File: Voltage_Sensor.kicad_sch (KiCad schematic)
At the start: 30 parts, among them U1 TLV9002QDRQ1

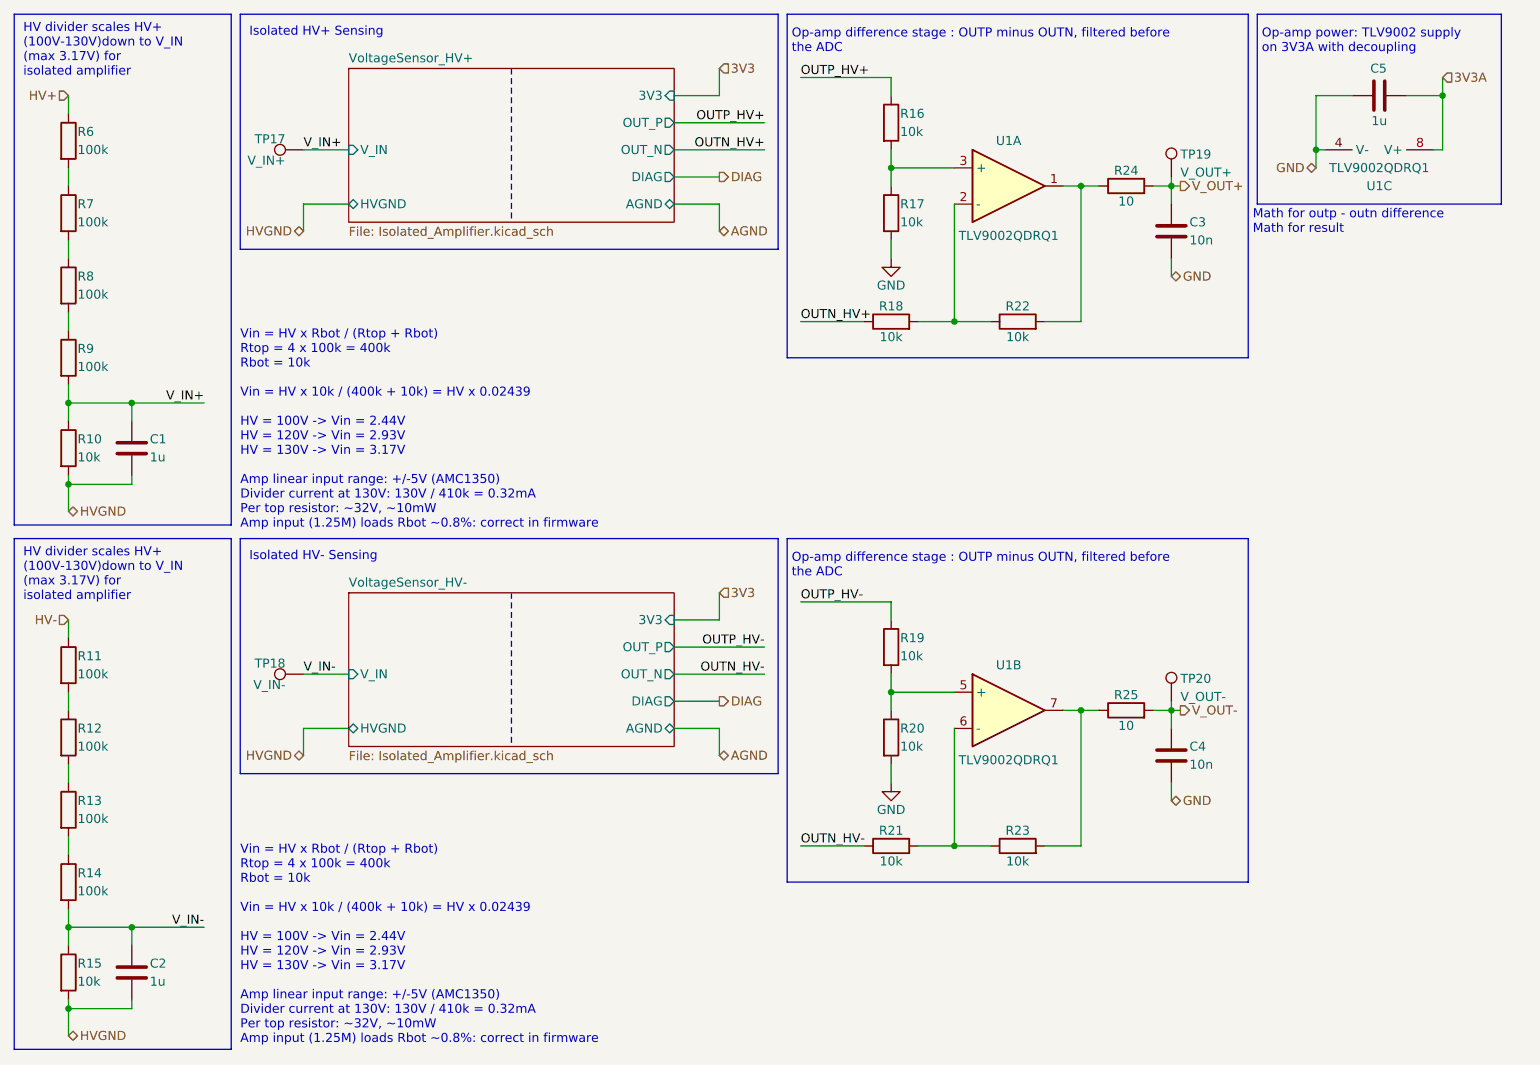
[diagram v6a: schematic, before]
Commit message: updated voltage divider to amc3311
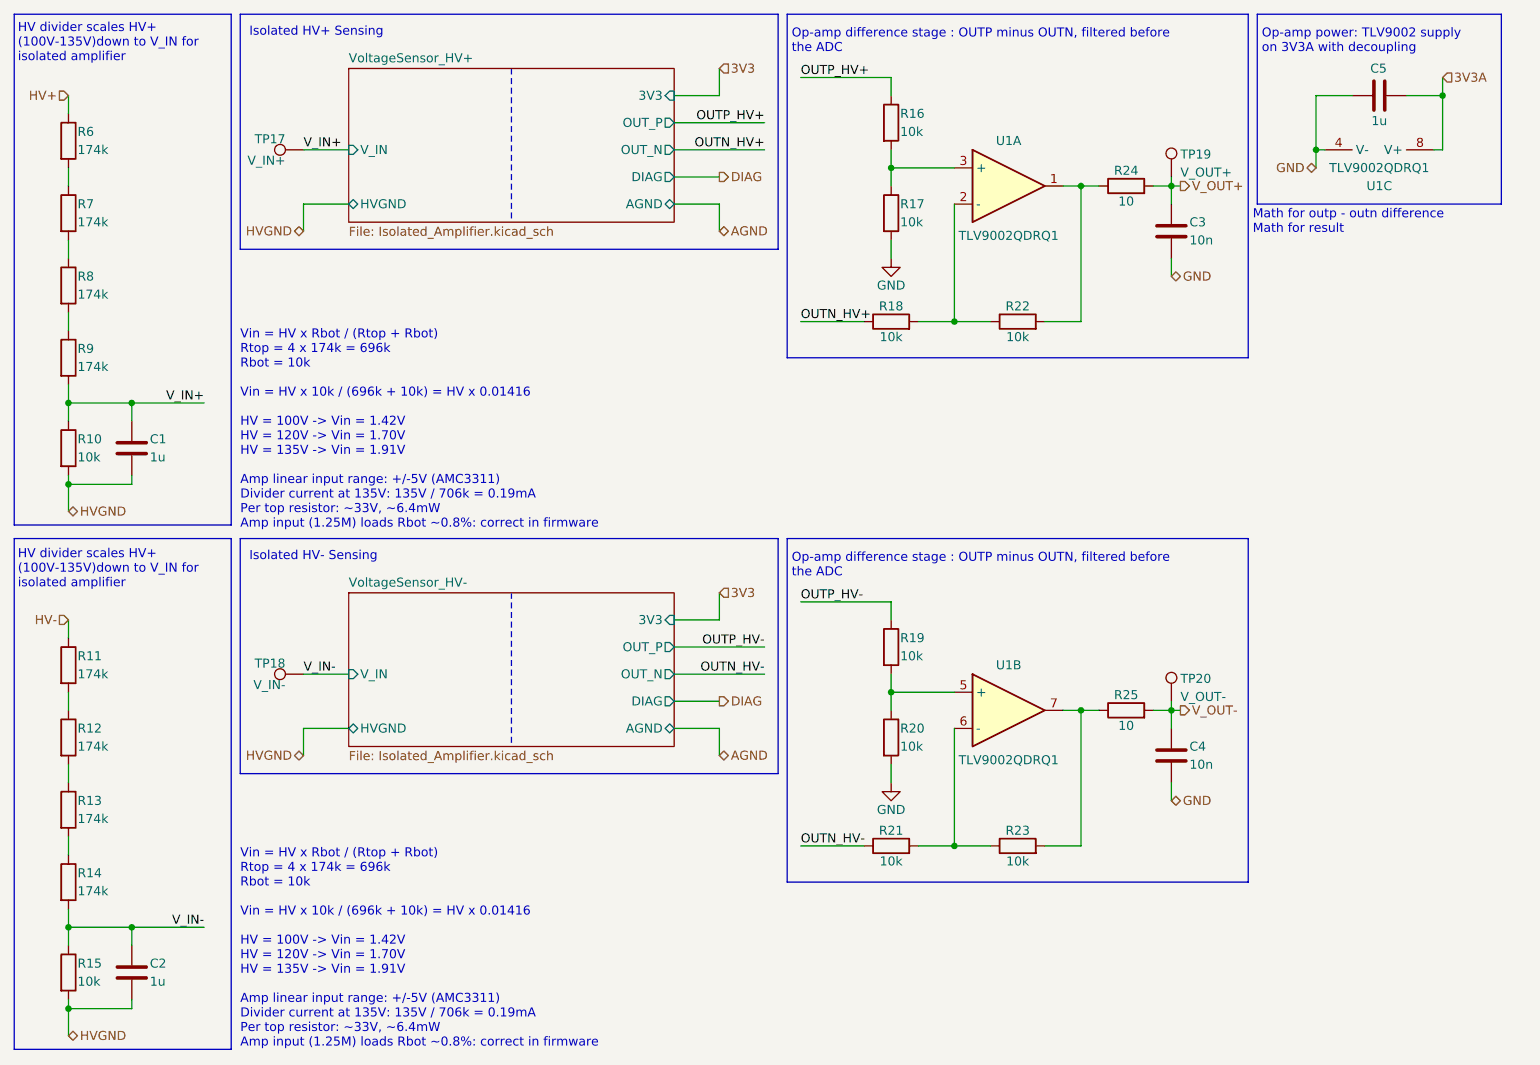
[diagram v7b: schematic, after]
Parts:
- R11, R12, R13, R14, R6, R7, R8, R9: value 100k -> 174k
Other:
- note added: "HV divider scales HV+ (100V-135V)down to V_IN for isolated amplifier"
- note added: "Vin = HV x Rbot / (Rtop + Rbot) Rtop = 4 x 174k = 696k Rbot = 10k Vin = HV x 10k / (696k + 10k) = HV x 0.01416 HV = 100V -> Vin = 1.42V HV = 120V -> Vin = 1.70V HV = 135V -> Vin = 1.91V Amp linear input range: +/-5V (AMC3311) Divider current at 135V: 135V / 706k = 0.19mA Per top resistor: ~33V, ~6.4mW Amp input (1.25M) loads Rbot ~0.8%: correct in firmware"
- note removed: "HV divider scales HV+ (100V-130V)down to V_IN (max 3.17V) for isolated amplifier"
- note removed: "Vin = HV x Rbot / (Rtop + Rbot) Rtop = 4 x 100k = 400k Rbot = 10k Vin = HV x 10k / (400k + 10k) = HV x 0.02439 HV = 100V -> Vin = 2.44V HV = 120V -> Vin = 2.93V HV = 130V -> Vin = 3.17V Amp linear input range: +/-5V (AMC1350) Divider current at 130V: 130V / 410k = 0.32mA Per top resistor: ~32V, ~10mW Amp input (1.25M) loads Rbot ~0.8%: correct in firmware"
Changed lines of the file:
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@@
 		)
 	)
-	(text "HV divider scales HV+ \n(100V-130V)down to V_IN \n(max 3.17V) for \nisolated amplifier"
+	(text "HV divider scales HV+ \n(100V-135V)down to V_IN for \nisolated amplifier"
 		(exclude_from_sim no)
-		(at 15.24 19.05 0)
+		(at 14.478 18.034 0)
 		(effects
 			(font
@@
 		)
 	)
-	(text "Vin = HV x Rbot / (Rtop + Rbot)\nRtop = 4 x 100k = 400k\nRbot = 10k\n\nVin = HV x 10k / (400k + 10k) = HV x 0.02439\n\nHV = 100V -> Vin = 2.44V\nHV = 120V -> Vin = 2.93V\nHV = 130V -> Vin = 3.17V\n\nAmp linear input range: +/-5V (AMC1350)\nDivider current at 130V: 130V / 410k = 0.32mA\nPer top resistor: ~32V, ~10mW\nAmp input (1.25M) loads Rbot ~0.8%: correct in firmware"
+	(text "Vin = HV x Rbot / (Rtop + Rbot)\nRtop = 4 x 174k = 696k\nRbot = 10k\n\nVin = HV x 10k / (696k + 10k) = HV x 0.01416\n\nHV = 100V -> Vin = 1.42V\nHV = 120V -> Vin = 1.70V\nHV = 135V -> Vin = 1.91V\n\nAmp linear input range: +/-5V (AMC3311)\nDivider current at 135V: 135V / 706k = 0.19mA\nPer top resistor: ~33V, ~6.4mW\nAmp input (1.25M) loads Rbot ~0.8%: correct in firmware"
 		(exclude_from_sim no)
-		(at 45.72 158.75 0)
+		(at 45.72 159.258 0)
 		(effects
 			(font
@@
 		)
 	)
-	(text "HV divider scales HV+ \n(100V-130V)down to V_IN \n(max 3.17V) for \nisolated amplifier"
+	(text "Vin = HV x Rbot / (Rtop + Rbot)\nRtop = 4 x 174k = 696k\nRbot = 10k\n\nVin = HV x 10k / (696k + 10k) = HV x 0.01416\n\nHV = 100V -> Vin = 1.42V\nHV = 120V -> Vin = 1.70V\nHV = 135V -> Vin = 1.91V\n\nAmp linear input range: +/-5V (AMC3311)\nDivider current at 135V: 135V / 706k = 0.19mA\nPer top resistor: ~33V, ~6.4mW\nAmp input (1.25M) loads Rbot ~0.8%: correct in firmware"
 		(exclude_from_sim no)
-		(at 15.24 92.71 0)
+		(at 45.72 86.36 0)
 		(effects
 			(font
 				(size 1.27 1.27)
 			)
-			(justify left)
+			(justify left bottom)
 		)
 	)
-	(text "Vin = HV x Rbot / (Rtop + Rbot)\nRtop = 4 x 100k = 400k\nRbot = 10k\n\nVin = HV x 10k / (400k + 10k) = HV x 0.02439\n\nHV = 100V -> Vin = 2.44V\nHV = 120V -> Vin = 2.93V\nHV = 130V -> Vin = 3.17V\n\nAmp linear input range: +/-5V (AMC1350)\nDivider current at 130V: 130V / 410k = 0.32mA\nPer top resistor: ~32V, ~10mW\nAmp input (1.25M) loads Rbot ~0.8%: correct in firmware"
+	(text "Isolated HV+ Sensing"
 		(exclude_from_sim no)
-		(at 45.72 86.36 0)
+		(at 46.99 16.51 0)
 		(effects
 			(font
 				(size 1.27 1.27)
 			)
-			(justify left bottom)
+			(justify left)
 		)
 	)
-	(text "Isolated HV+ Sensing"
+	(text "HV divider scales HV+ \n(100V-135V)down to V_IN for \nisolated amplifier"
 		(exclude_from_sim no)
-		(at 46.99 16.51 0)
+		(at 14.478 91.948 0)
 		(effects
 			(font
@@
 			)
 		)
-		(property "Value" "100k"
+		(property "Value" "174k"
 			(at 22.86 116.84 0)
 			(show_name no)
@@
 				)
 				(path "/74d17fe6-68d4-4bd7-954a-e2bbb58b1f1e/c9d052f0-39c4-441f-8d4e-0430a3425be4"
-					(reference "R42")
+					(reference "R43")
 					(unit 1)
 				)
@@
 			)
 		)
-		(property "Value" "100k"
+		(property "Value" "174k"
 			(at 22.86 137.16 0)
 			(show_name no)
@@
 				)
 				(path "/74d17fe6-68d4-4bd7-954a-e2bbb58b1f1e/c9d052f0-39c4-441f-8d4e-0430a3425be4"
-					(reference "R44")
+					(reference "R45")
 					(unit 1)
 				)
@@
 			)
 		)
-		(property "Value" "100k"
+		(property "Value" "174k"
 			(at 22.86 63.5 0)
 			(show_name no)
@@
 				)
 				(path "/74d17fe6-68d4-4bd7-954a-e2bbb58b1f1e/c9d052f0-39c4-441f-8d4e-0430a3425be4"
-					(reference "R39")
+					(reference "R40")
 					(unit 1)
 				)
@@
 			)
 		)
-		(property "Value" "100k"
+		(property "Value" "174k"
 			(at 22.86 106.68 0)
 			(show_name no)
@@
 				)
 				(path "/74d17fe6-68d4-4bd7-954a-e2bbb58b1f1e/c9d052f0-39c4-441f-8d4e-0430a3425be4"
-					(reference "R41")
+					(reference "R42")
 					(unit 1)
 				)
@@
 			)
 		)
-		(property "Value" "100k"
+		(property "Value" "174k"
 			(at 22.86 127 0)
 			(show_name no)
@@
 				)
 				(path "/74d17fe6-68d4-4bd7-954a-e2bbb58b1f1e/c9d052f0-39c4-441f-8d4e-0430a3425be4"
-					(reference "R43")
+					(reference "R44")
 					(unit 1)
 				)
@@
 				)
 				(path "/74d17fe6-68d4-4bd7-954a-e2bbb58b1f1e/c9d052f0-39c4-441f-8d4e-0430a3425be4"
-					(reference "R45")
+					(reference "R46")
 					(unit 1)
 				)
@@
 				)
 				(path "/74d17fe6-68d4-4bd7-954a-e2bbb58b1f1e/c9d052f0-39c4-441f-8d4e-0430a3425be4"
-					(reference "R55")
+					(reference "R56")
 					(unit 1)
 				)
@@
 				)
 				(path "/74d17fe6-68d4-4bd7-954a-e2bbb58b1f1e/c9d052f0-39c4-441f-8d4e-0430a3425be4"
-					(reference "R52")
+					(reference "R53")
 					(unit 1)
 				)
@@
 			)
 		)
-		(property "Value" "100k"
+		(property "Value" "174k"
 			(at 22.86 53.34 0)
 			(show_name no)
@@
 				)
 				(path "/74d17fe6-68d4-4bd7-954a-e2bbb58b1f1e/c9d052f0-39c4-441f-8d4e-0430a3425be4"
-					(reference "R38")
+					(reference "R39")
 					(unit 1)
 				)
@@
 				)
 				(path "/74d17fe6-68d4-4bd7-954a-e2bbb58b1f1e/c9d052f0-39c4-441f-8d4e-0430a3425be4"
-					(reference "R48")
+					(reference "R49")
 					(unit 1)
 				)
@@
 				)
 				(path "/74d17fe6-68d4-4bd7-954a-e2bbb58b1f1e/c9d052f0-39c4-441f-8d4e-0430a3425be4"
-					(reference "R51")
+					(reference "R52")
 					(unit 1)
 				)
@@
 				)
 				(path "/74d17fe6-68d4-4bd7-954a-e2bbb58b1f1e/c9d052f0-39c4-441f-8d4e-0430a3425be4"
-					(reference "R47")
+					(reference "R48")
 					(unit 1)
 				)
@@
 			)
 		)
-		(property "Value" "100k"
+		(property "Value" "174k"
 			(at 22.86 33.02 0)
 			(show_name no)
@@
 				)
 				(path "/74d17fe6-68d4-4bd7-954a-e2bbb58b1f1e/c9d052f0-39c4-441f-8d4e-0430a3425be4"
-					(reference "R36")
+					(reference "R37")
 					(unit 1)
 				)
@@
 				)
 				(path "/74d17fe6-68d4-4bd7-954a-e2bbb58b1f1e/c9d052f0-39c4-441f-8d4e-0430a3425be4"
-					(reference "R54")
+					(reference "R55")
 					(unit 1)
 				)
@@
 				)
 				(path "/74d17fe6-68d4-4bd7-954a-e2bbb58b1f1e/c9d052f0-39c4-441f-8d4e-0430a3425be4"
-					(reference "R49")
+					(reference "R50")
 					(unit 1)
 				)
@@
 				)
 				(path "/74d17fe6-68d4-4bd7-954a-e2bbb58b1f1e/c9d052f0-39c4-441f-8d4e-0430a3425be4"
-					(reference "R53")
+					(reference "R54")
 					(unit 1)
 				)
@@
 			)
 		)
-		(property "Value" "100k"
+		(property "Value" "174k"
 			(at 22.86 43.18 0)
 			(show_name no)
@@
 				)
 				(path "/74d17fe6-68d4-4bd7-954a-e2bbb58b1f1e/c9d052f0-39c4-441f-8d4e-0430a3425be4"
-					(reference "R37")
+					(reference "R38")
 					(unit 1)
 				)
@@
 				)
 				(path "/74d17fe6-68d4-4bd7-954a-e2bbb58b1f1e/c9d052f0-39c4-441f-8d4e-0430a3425be4"
-					(reference "R46")
+					(reference "R47")
 					(unit 1)
 				)
@@
 				)
 				(path "/74d17fe6-68d4-4bd7-954a-e2bbb58b1f1e/c9d052f0-39c4-441f-8d4e-0430a3425be4"
-					(reference "R50")
+					(reference "R51")
 					(unit 1)
 				)
@@
 				)
 				(path "/74d17fe6-68d4-4bd7-954a-e2bbb58b1f1e/c9d052f0-39c4-441f-8d4e-0430a3425be4"
-					(reference "R40")
+					(reference "R41")
 					(unit 1)
 				)

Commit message: fixed hv placement
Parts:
- TP15: renamed from TP17; footprint TestPoint:TestPoint_Loop_D1.80mm_Drill1.0mm_Beaded -> TestPoint:TestPoint_THTPad_D3.0mm_Drill1.5mm
- TP16: renamed from TP18; footprint TestPoint:TestPoint_Loop_D1.80mm_Drill1.0mm_Beaded -> TestPoint:TestPoint_THTPad_D3.0mm_Drill1.5mm
- TP17: renamed from TP19; footprint TestPoint:TestPoint_Loop_D1.80mm_Drill1.0mm_Beaded -> TestPoint:TestPoint_THTPad_D3.0mm_Drill1.5mm
- TP18: renamed from TP20; footprint TestPoint:TestPoint_Loop_D1.80mm_Drill1.0mm_Beaded -> TestPoint:TestPoint_THTPad_D3.0mm_Drill1.5mm
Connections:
- net 3V3A is gone; now on net 3V3: C5.1, U1.8 (V+)
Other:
- sheet VoltageSensor_HV+ ports: added none; removed AGND
- sheet VoltageSensor_HV- ports: added none; removed AGND
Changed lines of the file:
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@@
 	(wire
 		(pts
-			(xy 113.03 40.64) (xy 106.68 40.64)
-		)
-		(stroke
-			(width 0)
-			(type default)
-		)
-	)
-	(wire
-		(pts
 			(xy 21.59 45.72) (xy 21.59 48.26)
 		)
@@
 	(wire
 		(pts
-			(xy 113.03 114.3) (xy 113.03 118.11)
-		)
-		(stroke
-			(width 0)
-			(type default)
-		)
-	)
-	(wire
-		(pts
 			(xy 54.61 114.3) (xy 60.96 114.3)
 		)
@@
 	(wire
 		(pts
-			(xy 113.03 40.64) (xy 113.03 44.45)
-		)
-		(stroke
-			(width 0)
-			(type default)
-		)
-	)
-	(wire
-		(pts
 			(xy 163.83 130.81) (xy 158.75 130.81)
 		)
@@
 	(wire
 		(pts
-			(xy 113.03 114.3) (xy 106.68 114.3)
-		)
-		(stroke
-			(width 0)
-			(type default)
-		)
-	)
-	(wire
-		(pts
 			(xy 54.61 40.64) (xy 54.61 44.45)
 		)
@@
 		)
 	)
-	(hierarchical_label "3V3A"
+	(hierarchical_label "3V3"
 		(shape input)
 		(at 214.63 22.86 0)
@@
 		)
 	)
-	(hierarchical_label "AGND"
-		(shape bidirectional)
-		(at 113.03 118.11 0)
-		(effects
-			(font
-				(size 1.27 1.27)
-			)
-			(justify left)
-		)
-	)
 	(hierarchical_label "HVGND"
 		(shape bidirectional)
@@
 		)
 	)
-	(hierarchical_label "AGND"
-		(shape bidirectional)
-		(at 113.03 44.45 0)
-		(effects
-			(font
-				(size 1.27 1.27)
-			)
-			(justify left)
-		)
-	)
 	(hierarchical_label "HV-"
 		(shape input)
@@
 		(in_pos_files yes)
 		(dnp no)
-		(property "Reference" "TP18"
+		(property "Reference" "TP16"
 			(at 52.07 105.918 90)
 			(show_name no)
@@
 			)
 		)
-		(property "Footprint" "TestPoint:TestPoint_Loop_D1.80mm_Drill1.0mm_Beaded"
+		(property "Footprint" "TestPoint:TestPoint_THTPad_D3.0mm_Drill1.5mm"
 			(at 49.53 106.68 0)
 			(hide yes)
@@
 			(project "PS-PrechargeBoard"
 				(path "/74d17fe6-68d4-4bd7-954a-e2bbb58b1f1e/6627985a-aef4-4302-9d05-a969136ea8f4"
-					(reference "TP18")
+					(reference "TP16")
 					(unit 1)
 				)
 				(path "/74d17fe6-68d4-4bd7-954a-e2bbb58b1f1e/c9d052f0-39c4-441f-8d4e-0430a3425be4"
-					(reference "TP22")
+					(reference "TP20")
 					(unit 1)
 				)
@@
 		(in_pos_files yes)
 		(dnp no)
-		(property "Reference" "TP17"
+		(property "Reference" "TP15"
 			(at 52.07 32.258 90)
 			(show_name no)
@@
 			)
 		)
-		(property "Footprint" "TestPoint:TestPoint_Loop_D1.80mm_Drill1.0mm_Beaded"
+		(property "Footprint" "TestPoint:TestPoint_THTPad_D3.0mm_Drill1.5mm"
 			(at 49.53 33.02 0)
 			(hide yes)
@@
 			(project "PS-PrechargeBoard"
 				(path "/74d17fe6-68d4-4bd7-954a-e2bbb58b1f1e/6627985a-aef4-4302-9d05-a969136ea8f4"
-					(reference "TP17")
+					(reference "TP15")
 					(unit 1)
 				)
 				(path "/74d17fe6-68d4-4bd7-954a-e2bbb58b1f1e/c9d052f0-39c4-441f-8d4e-0430a3425be4"
-					(reference "TP21")
+					(reference "TP19")
 					(unit 1)
 				)
@@
 		(in_pos_files yes)
 		(dnp no)
-		(property "Reference" "TP20"
+		(property "Reference" "TP18"
 			(at 177.8 107.315 0)
 			(show_name no)
@@
 			)
 		)
-		(property "Footprint" "TestPoint:TestPoint_Loop_D1.80mm_Drill1.0mm_Beaded"
+		(property "Footprint" "TestPoint:TestPoint_THTPad_D3.0mm_Drill1.5mm"
 			(at 176.53 105.41 0)
 			(hide yes)
@@
 			(project "PS-PrechargeBoard"
 				(path "/74d17fe6-68d4-4bd7-954a-e2bbb58b1f1e/6627985a-aef4-4302-9d05-a969136ea8f4"
-					(reference "TP20")
+					(reference "TP18")
 					(unit 1)
 				)
 				(path "/74d17fe6-68d4-4bd7-954a-e2bbb58b1f1e/c9d052f0-39c4-441f-8d4e-0430a3425be4"
-					(reference "TP24")
+					(reference "TP22")
 					(unit 1)
 				)
@@
 		(in_pos_files yes)
 		(dnp no)
-		(property "Reference" "#PWR030"
+		(property "Reference" "#PWR026"
 			(at 137.16 128.27 0)
 			(hide yes)
@@
 			(project "PS-PrechargeBoard"
 				(path "/74d17fe6-68d4-4bd7-954a-e2bbb58b1f1e/6627985a-aef4-4302-9d05-a969136ea8f4"
-					(reference "#PWR030")
+					(reference "#PWR026")
 					(unit 1)
 				)
 				(path "/74d17fe6-68d4-4bd7-954a-e2bbb58b1f1e/c9d052f0-39c4-441f-8d4e-0430a3425be4"
-					(reference "#PWR032")
+					(reference "#PWR028")
 					(unit 1)
 				)
@@
 		(in_pos_files yes)
 		(dnp no)
-		(property "Reference" "TP19"
+		(property "Reference" "TP17"
 			(at 177.8 33.655 0)
 			(show_name no)
@@
 			)
 		)
-		(property "Footprint" "TestPoint:TestPoint_Loop_D1.80mm_Drill1.0mm_Beaded"
+		(property "Footprint" "TestPoint:TestPoint_THTPad_D3.0mm_Drill1.5mm"
 			(at 176.53 31.75 0)
 			(hide yes)
@@
 			(project "PS-PrechargeBoard"
 				(path "/74d17fe6-68d4-4bd7-954a-e2bbb58b1f1e/6627985a-aef4-4302-9d05-a969136ea8f4"
-					(reference "TP19")
+					(reference "TP17")
 					(unit 1)
 				)
 				(path "/74d17fe6-68d4-4bd7-954a-e2bbb58b1f1e/c9d052f0-39c4-441f-8d4e-0430a3425be4"
-					(reference "TP23")
+					(reference "TP21")
 					(unit 1)
 				)
@@
 		(in_pos_files yes)
 		(dnp no)
-		(property "Reference" "#PWR029"
+		(property "Reference" "#PWR025"
 			(at 137.16 54.61 0)
 			(hide yes)
@@
 			(project "PS-PrechargeBoard"
 				(path "/74d17fe6-68d4-4bd7-954a-e2bbb58b1f1e/6627985a-aef4-4302-9d05-a969136ea8f4"
-					(reference "#PWR029")
+					(reference "#PWR025")
 					(unit 1)
 				)
 				(path "/74d17fe6-68d4-4bd7-954a-e2bbb58b1f1e/c9d052f0-39c4-441f-8d4e-0430a3425be4"
-					(reference "#PWR031")
+					(reference "#PWR027")
 					(unit 1)
 				)
@@
 			)
 		)
-		(pin "AGND" bidirectional
-			(at 106.68 114.3 0)
-			(effects
-				(font
-					(size 1.27 1.27)
-				)
-				(justify right)
-			)
-		)
 		(pin "HVGND" bidirectional
 			(at 60.96 114.3 180)
@@
 			(effects
 				(font
-					(size 1.27 1.27)
-				)
-				(justify right)
-			)
-		)
-		(pin "AGND" bidirectional
-			(at 106.68 40.64 0)
-			(effects
-				(font
